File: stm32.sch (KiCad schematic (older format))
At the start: 30 parts, among them J6 USB_C_Receptacle_USB2.0, U3 STM32F205RBTx, U4 OLED_0.96\"_SSD1306, Y2 8M

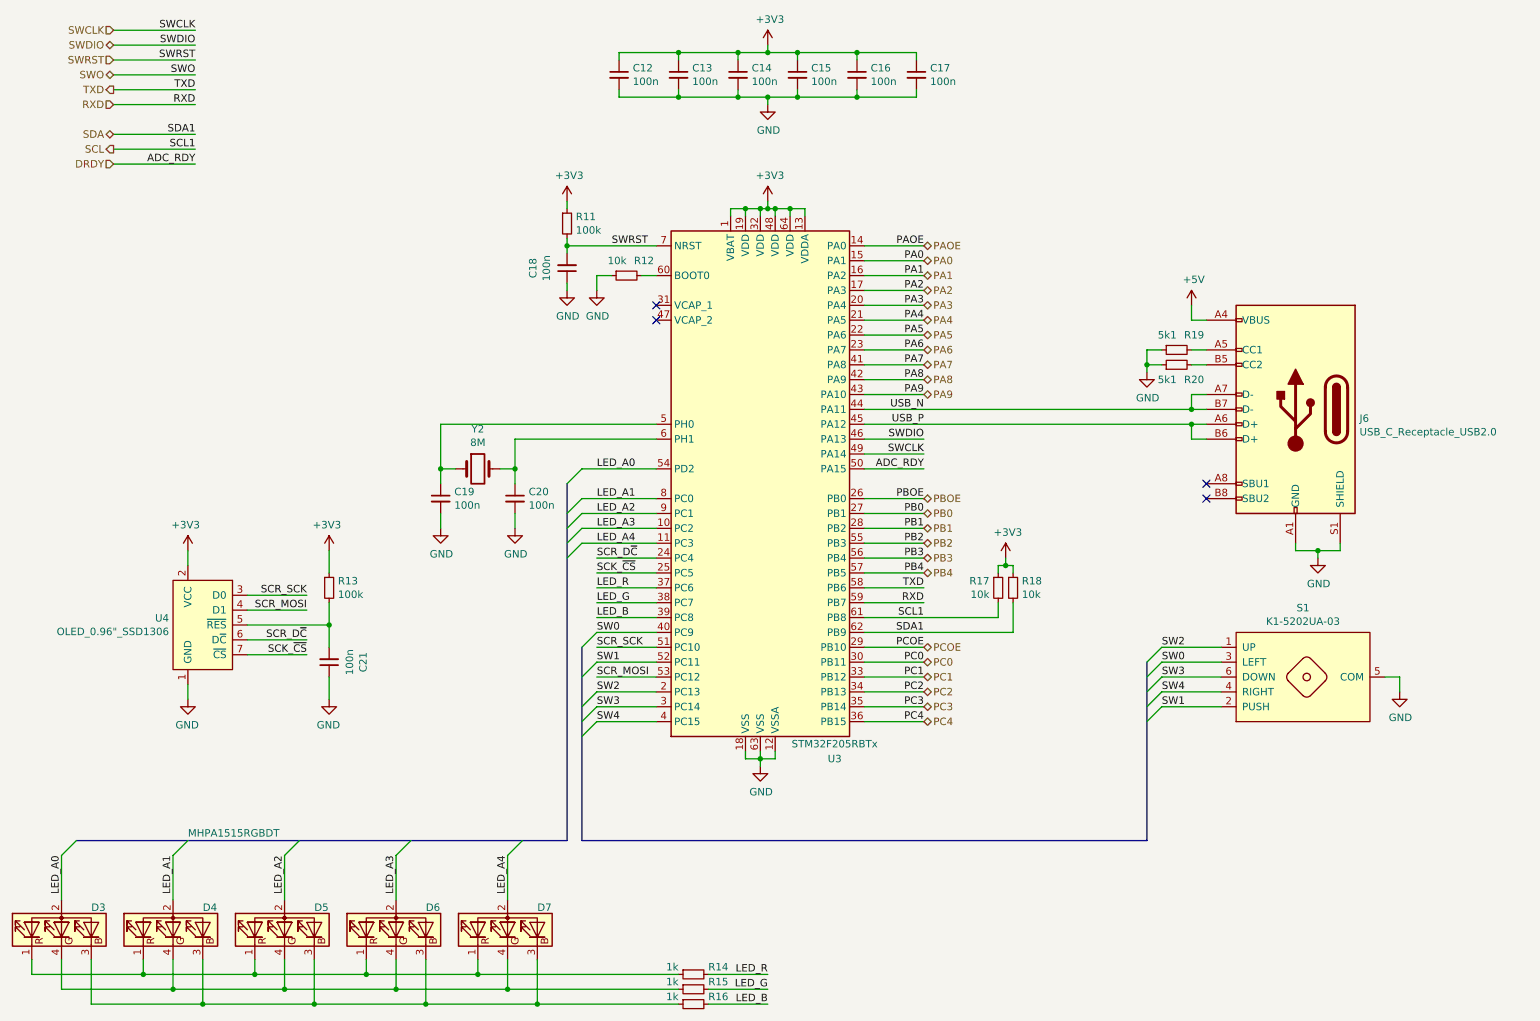
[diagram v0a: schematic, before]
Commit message: sch, pcb: Add USB hub to have a single USB port
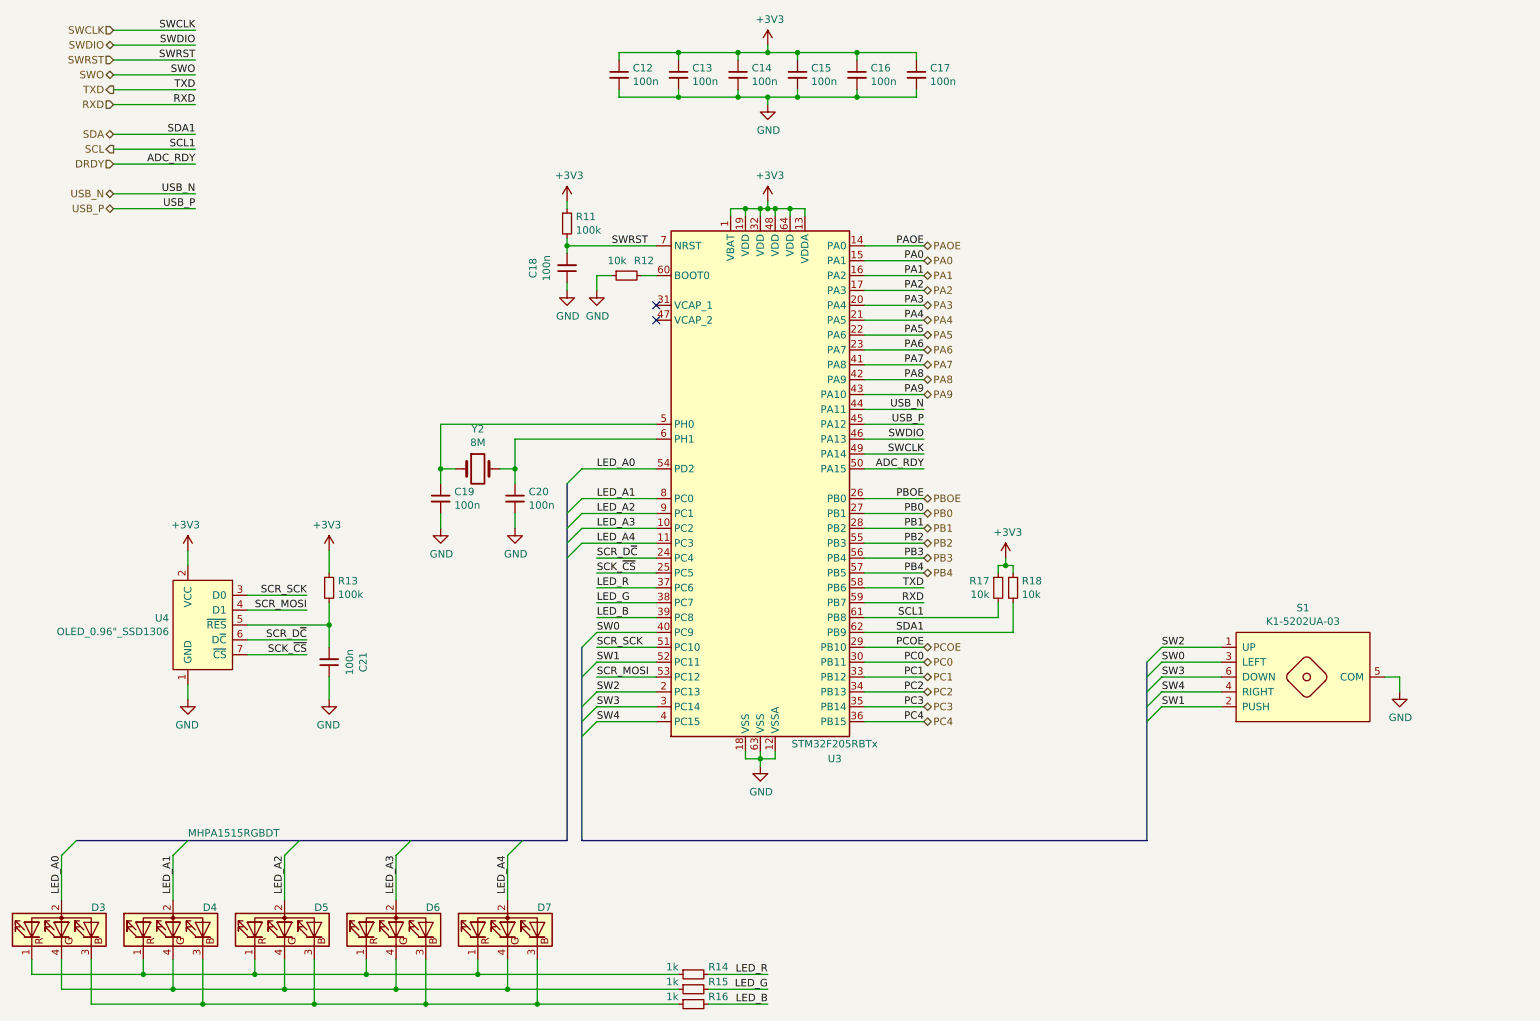
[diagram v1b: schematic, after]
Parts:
- removed J6: USB_C_Receptacle_USB2.0, antboard:USB_C_Receptacle_Palconn_UTC16-G, symbol Connector:USB_C_Receptacle_USB2.0
- removed R19, R20: 5k1, Resistor_SMD:R_0603_1608Metric, symbol Device:R_Small
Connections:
- no-connect marks 4 -> 2
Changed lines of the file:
@@
 EESchema Schematic File Version 4
+LIBS:antboard-cache
 EELAYER 30 0
 EELAYER END
 $Descr A4 11693 8268
 encoding utf-8
-Sheet 3 5
+Sheet 3 6
 Title ""
 Date ""
@@
 	1    0    0    -1
 $EndComp
-$Comp
-L Device:Crystal Y?
-U 1 1 5DFC7A1F
-P 3800 3950
-AR Path="/5DF7E971/5DFC7A1F" Ref="Y?"  Part="1"
-AR Path="/5DFC2583/5DFC7A1F" Ref="Y2"  Part="1"
-F 0 "Y2" H 3800 4218 50  0000 C CNN
-F 1 "8M" H 3800 4127 50  0000 C CNN
-F 2 "Crystal:Crystal_HC49-4H_Vertical" H 3800 3950 50  0001 C CNN
-F 3 "~" H 3800 3950 50  0001 C CNN
-	1    3800 3950
-	1    0    0    -1
-$EndComp
-$Comp
-L Device:C_Small C?
-U 1 1 5DFC7A25
-P 3550 4150
-AR Path="/5DF7E971/5DFC7A25" Ref="C?"  Part="1"
-AR Path="/5DFC2583/5DFC7A25" Ref="C19"  Part="1"
-F 0 "C19" H 3458 4196 50  0000 R CNN
-F 1 "100n" H 3458 4105 50  0000 R CNN
-F 2 "Capacitor_SMD:C_0603_1608Metric" H 3550 4150 50  0001 C CNN
-F 3 "~" H 3550 4150 50  0001 C CNN
-	1    3550 4150
-	-1   0    0    -1
-$EndComp
-$Comp
-L Device:C_Small C?
-U 1 1 5DFC7A2B
-P 4050 4150
-AR Path="/5DF7E971/5DFC7A2B" Ref="C?"  Part="1"
-AR Path="/5DFC2583/5DFC7A2B" Ref="C20"  Part="1"
-F 0 "C20" H 3958 4196 50  0000 R CNN
-F 1 "100n" H 3958 4105 50  0000 R CNN
-F 2 "Capacitor_SMD:C_0603_1608Metric" H 4050 4150 50  0001 C CNN
-F 3 "~" H 4050 4150 50  0001 C CNN
-	1    4050 4150
-	-1   0    0    -1
-$EndComp
-Wire Wire Line
-	5000 3750 4050 3750
-Wire Wire Line
-	4050 3750 4050 3950
-Wire Wire Line
-	5000 3650 3550 3650
-Wire Wire Line
-	3550 3650 3550 3950
-Wire Wire Line
-	3550 3950 3650 3950
-Connection ~ 3550 3950
-Wire Wire Line
-	3550 3950 3550 4050
-Wire Wire Line
-	3950 3950 4050 3950
-Wire Wire Line
-	4050 3950 4050 4050
-Connection ~ 4050 3950
-$Comp
-L power:GND #PWR?
-U 1 1 5DFC7A3B
-P 4050 4350
-AR Path="/5DF7E971/5DFC7A3B" Ref="#PWR?"  Part="1"
-AR Path="/5DFC2583/5DFC7A3B" Ref="#PWR0122"  Part="1"
-F 0 "#PWR0122" H 4050 4100 50  0001 C CNN
-F 1 "GND" H 4055 4177 50  0000 C CNN
-F 2 "" H 4050 4350 50  0001 C CNN
-F 3 "" H 4050 4350 50  0001 C CNN
-	1    4050 4350
-	1    0    0    -1
-$EndComp
-$Comp
-L power:GND #PWR?
-U 1 1 5DFC7A41
-P 3550 4350
-AR Path="/5DF7E971/5DFC7A41" Ref="#PWR?"  Part="1"
-AR Path="/5DFC2583/5DFC7A41" Ref="#PWR0123"  Part="1"
-F 0 "#PWR0123" H 3550 4100 50  0001 C CNN
-F 1 "GND" H 3555 4177 50  0000 C CNN
-F 2 "" H 3550 4350 50  0001 C CNN
-F 3 "" H 3550 4350 50  0001 C CNN
-	1    3550 4350
-	1    0    0    -1
-$EndComp
-Wire Wire Line
-	3550 4250 3550 4350
-Wire Wire Line
-	4050 4250 4050 4350
 $Comp
 L power:+3V3 #PWR0124
@@
 NoConn ~ 5000 2850
 NoConn ~ 5000 2950
-$Comp
-L Connector:USB_C_Receptacle_USB2.0 J6
-U 1 1 5DECBA68
-P 9300 3550
-F 0 "J6" H 8870 3489 50  0000 R CNN
-F 1 "USB_C_Receptacle_USB2.0" H 8870 3398 50  0000 R CNN
-F 2 "antboard:USB_C_Receptacle_Palconn_UTC16-G" H 9450 3550 50  0001 C CNN
-F 3 "https://www.usb.org/sites/default/files/documents/usb_type-c.zip" H 9450 3550 50  0001 C CNN
-	1    9300 3550
-	-1   0    0    -1
-$EndComp
 Text Label 6800 3550 2    50   ~ 0
 USB_N
 Text Label 6800 3650 2    50   ~ 0
 USB_P
-Wire Wire Line
-	6400 3550 8600 3550
-Wire Wire Line
-	6400 3650 8600 3650
-Wire Wire Line
-	8700 3450 8600 3450
-Wire Wire Line
-	8600 3450 8600 3550
-Connection ~ 8600 3550
-Wire Wire Line
-	8600 3550 8700 3550
-Wire Wire Line
-	8600 3650 8600 3750
-Wire Wire Line
-	8600 3750 8700 3750
-Connection ~ 8600 3650
-Wire Wire Line
-	8600 3650 8700 3650
-NoConn ~ 8700 4050
-NoConn ~ 8700 4150
-$Comp
-L Device:R_Small R?
-U 1 1 5DEF366C
-P 8500 3150
-AR Path="/5DF7E971/5DEF366C" Ref="R?"  Part="1"
-AR Path="/5DFC2583/5DEF366C" Ref="R19"  Part="1"
-F 0 "R19" V 8400 3100 50  0000 R CNN
-F 1 "5k1" V 8400 3150 50  0000 L CNN
-F 2 "Resistor_SMD:R_0603_1608Metric" H 8500 3150 50  0001 C CNN
-F 3 "~" H 8500 3150 50  0001 C CNN
-	1    8500 3150
-	0    -1   1    0
-$EndComp
-$Comp
-L Device:R_Small R?
-U 1 1 5DEF4157
-P 8500 3250
-AR Path="/5DF7E971/5DEF4157" Ref="R?"  Part="1"
-AR Path="/5DFC2583/5DEF4157" Ref="R20"  Part="1"
-F 0 "R20" V 8400 3200 50  0000 R CNN
-F 1 "5k1" V 8400 3250 50  0000 L CNN
-F 2 "Resistor_SMD:R_0603_1608Metric" H 8500 3250 50  0001 C CNN
-F 3 "~" H 8500 3250 50  0001 C CNN
-	1    8500 3250
-	0    -1   -1   0
-$EndComp
-Wire Wire Line
-	8600 3150 8700 3150
-Wire Wire Line
-	8700 3250 8600 3250
-Wire Wire Line
-	8400 3150 8300 3150
-Wire Wire Line
-	8300 3150 8300 3250
-Wire Wire Line
-	8300 3250 8400 3250
-$Comp
-L power:GND #PWR06
-U 1 1 5DF03FFD
-P 8300 3300
-F 0 "#PWR06" H 8300 3050 50  0001 C CNN
-F 1 "GND" H 8305 3127 50  0000 C CNN
-F 2 "" H 8300 3300 50  0001 C CNN
-F 3 "" H 8300 3300 50  0001 C CNN
-	1    8300 3300
-	1    0    0    -1
-$EndComp
-Wire Wire Line
-	8300 3300 8300 3250
-Connection ~ 8300 3250
-$Comp
-L power:GND #PWR08
-U 1 1 5DF08A10
-P 9450 4550
-F 0 "#PWR08" H 9450 4300 50  0001 C CNN
-F 1 "GND" H 9455 4377 50  0000 C CNN
-F 2 "" H 9450 4550 50  0001 C CNN
-F 3 "" H 9450 4550 50  0001 C CNN
-	1    9450 4550
-	1    0    0    -1
-$EndComp
-Wire Wire Line
-	9300 4450 9300 4500
-Wire Wire Line
-	9300 4500 9450 4500
-Wire Wire Line
-	9600 4500 9600 4450
-Wire Wire Line
-	9450 4550 9450 4500
-Connection ~ 9450 4500
-Wire Wire Line
-	9450 4500 9600 4500
-$Comp
-L power:+5V #PWR07
-U 1 1 5DF12003
-P 8600 2850
-F 0 "#PWR07" H 8600 2700 50  0001 C CNN
-F 1 "+5V" H 8615 3023 50  0000 C CNN
-F 2 "" H 8600 2850 50  0001 C CNN
-F 3 "" H 8600 2850 50  0001 C CNN
-	1    8600 2850
-	1    0    0    -1
-$EndComp
-Wire Wire Line
-	8600 2850 8600 2950
-Wire Wire Line
-	8600 2950 8700 2950
 Wire Wire Line
 	5000 5050 4600 5050
@@
 Entry Wire Line
 	4400 4050 4500 3950
+Wire Wire Line
+	5000 3650 3550 3650
+Wire Wire Line
+	5000 3750 4050 3750
+Wire Wire Line
+	4050 4250 4050 4350
+Wire Wire Line
+	3550 4250 3550 4350
+$Comp
+L power:GND #PWR?
+U 1 1 5DFC7A41
+P 3550 4350
+AR Path="/5DF7E971/5DFC7A41" Ref="#PWR?"  Part="1"
+AR Path="/5DFC2583/5DFC7A41" Ref="#PWR0123"  Part="1"
+F 0 "#PWR0123" H 3550 4100 50  0001 C CNN
+F 1 "GND" H 3555 4177 50  0000 C CNN
+F 2 "" H 3550 4350 50  0001 C CNN
+F 3 "" H 3550 4350 50  0001 C CNN
+	1    3550 4350
+	1    0    0    -1
+$EndComp
+$Comp
+L power:GND #PWR?
+U 1 1 5DFC7A3B
+P 4050 4350
+AR Path="/5DF7E971/5DFC7A3B" Ref="#PWR?"  Part="1"
+AR Path="/5DFC2583/5DFC7A3B" Ref="#PWR0122"  Part="1"
+F 0 "#PWR0122" H 4050 4100 50  0001 C CNN
+F 1 "GND" H 4055 4177 50  0000 C CNN
+F 2 "" H 4050 4350 50  0001 C CNN
+F 3 "" H 4050 4350 50  0001 C CNN
+	1    4050 4350
+	1    0    0    -1
+$EndComp
+Wire Wire Line
+	4050 3950 4050 4050
+Wire Wire Line
+	3950 3950 4050 3950
+Wire Wire Line
+	3550 3950 3550 4050
+Wire Wire Line
+	3550 3950 3650 3950
+Connection ~ 3550 3950
+Wire Wire Line
+	3550 3650 3550 3950
+Connection ~ 4050 3950
+Wire Wire Line
+	4050 3750 4050 3950
+$Comp
+L Device:C_Small C?
+U 1 1 5DFC7A2B
+P 4050 4150
+AR Path="/5DF7E971/5DFC7A2B" Ref="C?"  Part="1"
+AR Path="/5DFC2583/5DFC7A2B" Ref="C20"  Part="1"
+F 0 "C20" H 3958 4196 50  0000 R CNN
+F 1 "100n" H 3958 4105 50  0000 R CNN
+F 2 "Capacitor_SMD:C_0603_1608Metric" H 4050 4150 50  0001 C CNN
+F 3 "~" H 4050 4150 50  0001 C CNN
+	1    4050 4150
+	-1   0    0    -1
+$EndComp
+$Comp
+L Device:C_Small C?
+U 1 1 5DFC7A25
+P 3550 4150
+AR Path="/5DF7E971/5DFC7A25" Ref="C?"  Part="1"
+AR Path="/5DFC2583/5DFC7A25" Ref="C19"  Part="1"
+F 0 "C19" H 3458 4196 50  0000 R CNN
+F 1 "100n" H 3458 4105 50  0000 R CNN
+F 2 "Capacitor_SMD:C_0603_1608Metric" H 3550 4150 50  0001 C CNN
+F 3 "~" H 3550 4150 50  0001 C CNN
+	1    3550 4150
+	-1   0    0    -1
+$EndComp
+$Comp
+L Device:Crystal Y?
+U 1 1 5DFC7A1F
+P 3800 3950
+AR Path="/5DF7E971/5DFC7A1F" Ref="Y?"  Part="1"
+AR Path="/5DFC2583/5DFC7A1F" Ref="Y2"  Part="1"
+F 0 "Y2" H 3800 4218 50  0000 C CNN
+F 1 "8M" H 3800 4127 50  0000 C CNN
+F 2 "Crystal:Crystal_HC49-4H_Vertical" H 3800 3950 50  0001 C CNN
+F 3 "~" H 3800 3950 50  0001 C CNN
+	1    3800 3950
+	1    0    0    -1
+$EndComp
+Wire Wire Line
+	1350 2100 1900 2100
+Text Label 1900 2100 2    50   ~ 0
+USB_N
+Wire Wire Line
+	1350 2200 1900 2200
+Text Label 1900 2200 2    50   ~ 0
+USB_P
+Text HLabel 1350 2100 0    50   BiDi ~ 0
+USB_N
+Text HLabel 1350 2200 0    50   BiDi ~ 0
+USB_P
+Wire Wire Line
+	6400 3550 6800 3550
+Wire Wire Line
+	6400 3650 6800 3650
 Wire Bus Line
 	4400 4050 4400 6450

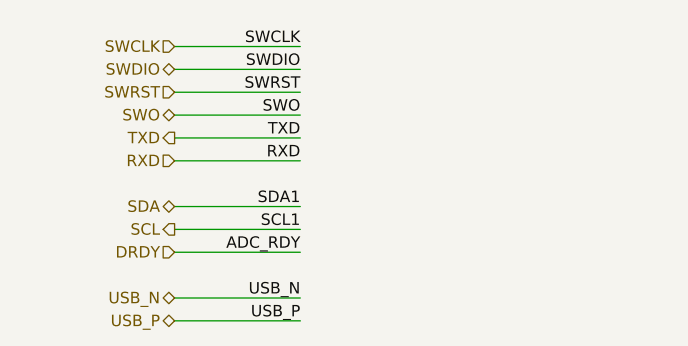
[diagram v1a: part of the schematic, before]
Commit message: Add solder bridges in line with the integrated JTAG
Just in case it does not works
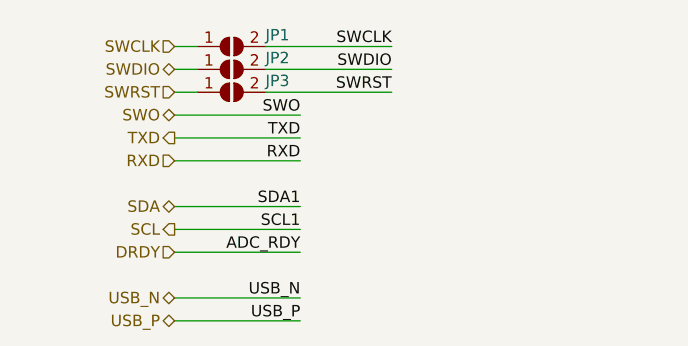
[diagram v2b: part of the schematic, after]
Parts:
- added JP1, JP2, JP3: SolderJumper_2_Bridged, Resistor_SMD:R_0603_1608Metric, symbol Jumper:SolderJumper_2_Open
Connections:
- net SWCLK: now also JP1.1 (A), JP1.2 (B)
- net SWDIO: now also JP2.1 (A), JP2.2 (B)
- net SWRST: now also JP3.1 (A), JP3.2 (B)
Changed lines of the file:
@@
 SWRST
 Wire Wire Line
-	1350 1000 1900 1000
-Text Label 1900 1000 2    50   ~ 0
+	1750 1000 2300 1000
+Text Label 2300 1000 2    50   ~ 0
 SWCLK
 Wire Wire Line
-	1350 1100 1900 1100
-Text Label 1900 1100 2    50   ~ 0
+	1750 1100 2300 1100
+Text Label 2300 1100 2    50   ~ 0
 SWDIO
 Wire Wire Line
-	1350 1200 1900 1200
-Text Label 1900 1200 2    50   ~ 0
+	1750 1200 2300 1200
+Text Label 2300 1200 2    50   ~ 0
 SWRST
 Text HLabel 1350 1000 0    50   Input ~ 0
@@
 Wire Wire Line
 	6400 3650 6800 3650
+$Comp
+L Jumper:SolderJumper_2_Open JP1
+U 1 1 5E13BB4F
+P 1600 1000
+F 0 "JP1" H 1800 1050 50  0000 C CNN
+F 1 "SolderJumper_2_Bridged" H 1600 1114 50  0001 C CNN
+F 2 "Resistor_SMD:R_0603_1608Metric" H 1600 1000 50  0001 C CNN
+F 3 "~" H 1600 1000 50  0001 C CNN
+	1    1600 1000
+	1    0    0    -1
+$EndComp
+$Comp
+L Jumper:SolderJumper_2_Open JP2
+U 1 1 5E154A90
+P 1600 1100
+F 0 "JP2" H 1800 1150 50  0000 C CNN
+F 1 "SolderJumper_2_Bridged" H 1600 1214 50  0001 C CNN
+F 2 "Resistor_SMD:R_0603_1608Metric" H 1600 1100 50  0001 C CNN
+F 3 "~" H 1600 1100 50  0001 C CNN
+	1    1600 1100
+	1    0    0    -1
+$EndComp
+$Comp
+L Jumper:SolderJumper_2_Open JP3
+U 1 1 5E154F58
+P 1600 1200
+F 0 "JP3" H 1800 1250 50  0000 C CNN
+F 1 "SolderJumper_2_Bridged" H 1600 1314 50  0001 C CNN
+F 2 "Resistor_SMD:R_0603_1608Metric" H 1600 1200 50  0001 C CNN
+F 3 "~" H 1600 1200 50  0001 C CNN
+	1    1600 1200
+	1    0    0    -1
+$EndComp
+Wire Wire Line
+	1350 1000 1450 1000
+Wire Wire Line
+	1450 1100 1350 1100
+Wire Wire Line
+	1350 1200 1450 1200
 Wire Bus Line
 	4400 4050 4400 6450

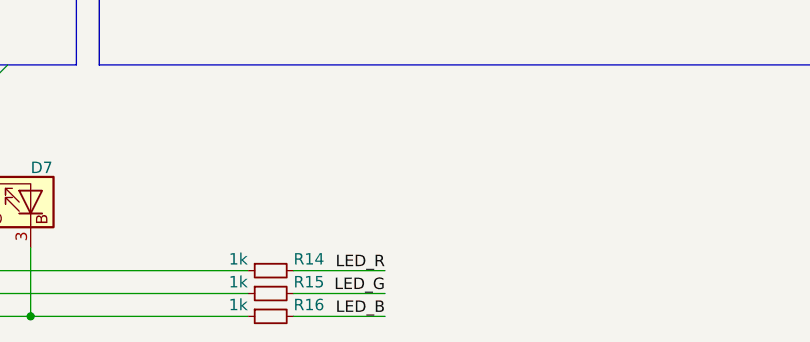
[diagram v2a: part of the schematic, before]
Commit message: sch: Fix LED resistors
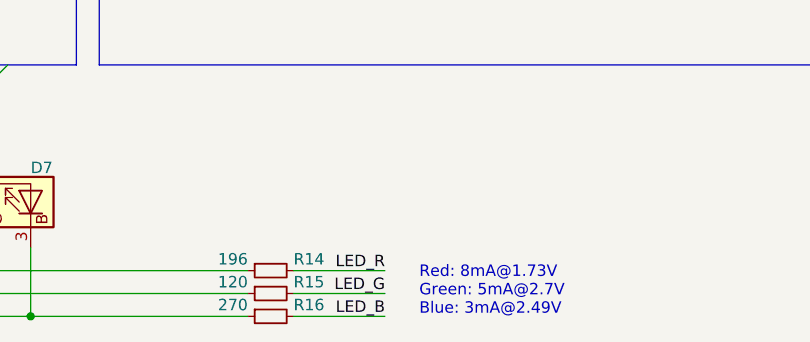
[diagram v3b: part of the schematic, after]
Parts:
- R14: value 1k -> 196
- R15: value 1k -> 120
- R16: value 1k -> 270
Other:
- note added: "Red: 8mA@1.73V\nGreen: 5mA@2.7V\nBlue: 3mA@2.49V"
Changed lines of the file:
@@
 AR Path="/5DFC2583/5E2945B4" Ref="R14"  Part="1"
 F 0 "R14" V 5200 7250 50  0000 R CNN
-F 1 "1k" V 5200 7450 50  0000 L CNN
+F 1 "196" V 5200 7450 50  0000 L CNN
 F 2 "Resistor_SMD:R_0603_1608Metric" H 5250 7350 50  0001 C CNN
 F 3 "~" H 5250 7350 50  0001 C CNN
@@
 AR Path="/5DFC2583/5E295ACD" Ref="R15"  Part="1"
 F 0 "R15" V 5200 7350 50  0000 R CNN
-F 1 "1k" V 5200 7550 50  0000 L CNN
+F 1 "120" V 5200 7550 50  0000 L CNN
 F 2 "Resistor_SMD:R_0603_1608Metric" H 5250 7450 50  0001 C CNN
 F 3 "~" H 5250 7450 50  0001 C CNN
@@
 AR Path="/5DFC2583/5E295D66" Ref="R16"  Part="1"
 F 0 "R16" V 5200 7450 50  0000 R CNN
-F 1 "1k" V 5200 7650 50  0000 L CNN
+F 1 "270" V 5200 7650 50  0000 L CNN
 F 2 "Resistor_SMD:R_0603_1608Metric" H 5250 7550 50  0001 C CNN
 F 3 "~" H 5250 7550 50  0001 C CNN
@@
 Wire Bus Line
 	8300 5250 8300 6450
+Text Notes 5900 7550 0    50   ~ 0
+Red: 8mA@1.73V\nGreen: 5mA@2.7V\nBlue: 3mA@2.49V
 $EndSCHEMATC
